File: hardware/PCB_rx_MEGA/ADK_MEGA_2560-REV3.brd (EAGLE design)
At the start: 9 parts

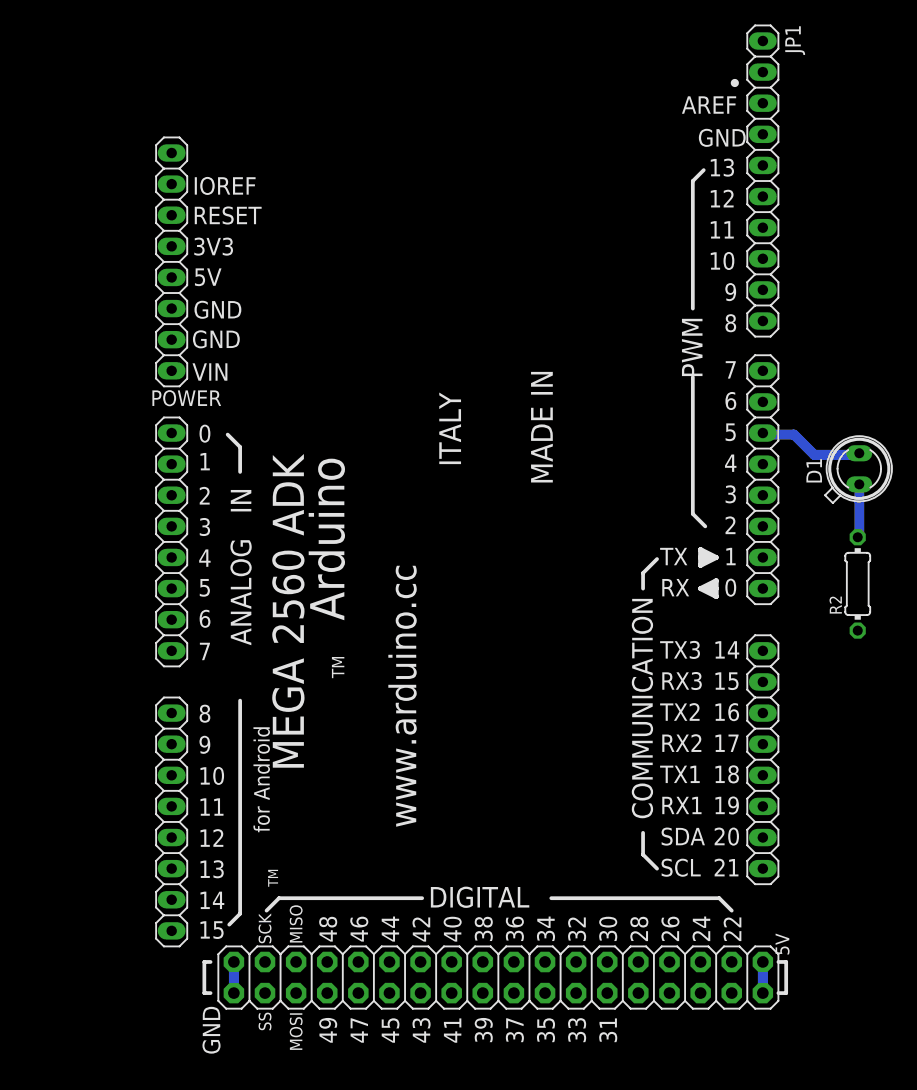
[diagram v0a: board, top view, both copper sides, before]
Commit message: Se añade modulo de comunicaciones junto con regulador al diseño de la shield para el nodo central
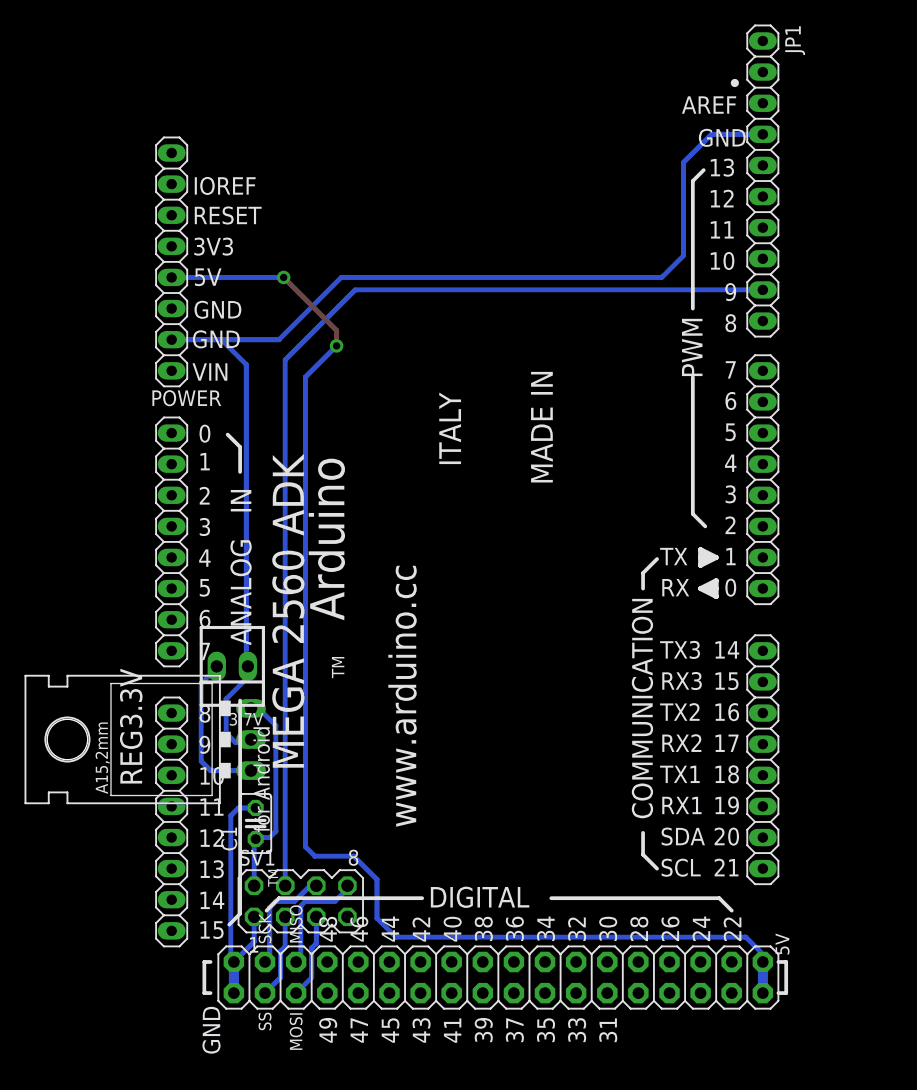
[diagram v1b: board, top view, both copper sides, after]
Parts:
- removed D1: SFH482, led:SFH482
- removed R2: (no value), eagle-ltspice:0204/7
- added 3.7V: 22-23-2021, con-molex:22-23-2021
- added C1: (no value), rcl:C025-025X050
- added REG3.3V: (no value), v-reg:78XXL
- added SV1: (no value), con-lstb:MA04-2
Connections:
- removed net N$2: D1.K, PWML.6
- removed net N$3: D1.A, R2.2
- new net 3.3V: C1.1, REG3.3V.OUT, SV1.2
- new net N$1: SV1.3, XIO.34
- new net N$5: SV1.5, XIO.32
- new net N$6: JP1.9, SV1.4
- new net N$7: SV1.6, XIO.33
- new net N$8: SV1.8, XIO.31
- new net N$9: 3.7V.2, REG3.3V.IN
- net GND: now also 3.7V.1, C1.2, REG3.3V.GND, SV1.1; no longer R2.1
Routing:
- net GND: track 2.90 -> 121.6 mm
- net VCC: track 2.54 -> 104.5 mm, vias 0 -> 2
- net N$6: track 0.00 -> 84.3 mm
- net 3.3V: track 0.00 -> 17.0 mm
- net N$9: track 0.00 -> 12.7 mm
- net N$8: track 0.00 -> 9.37 mm
- net N$7: track 0.00 -> 9.15 mm
- net N$2: track 8.66 -> 0.00 mm
- net N$1: track 0.00 -> 6.91 mm
- net N$5: track 0.00 -> 6.91 mm
- net N$3: track 4.37 -> 0.00 mm
